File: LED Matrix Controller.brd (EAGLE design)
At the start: 76.2 x 50.8 mm, 5 parts, among them CN1 LED OUT, CN2 5V PWR, U1 328P

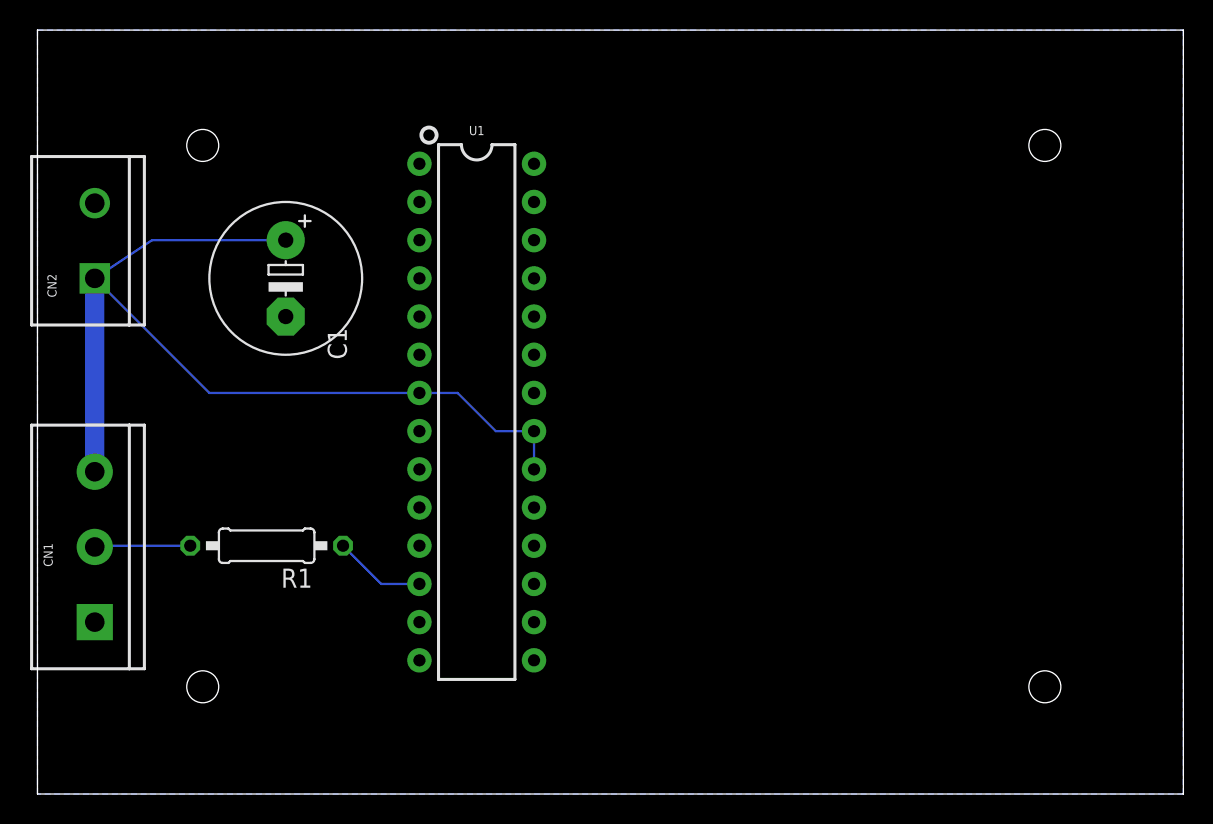
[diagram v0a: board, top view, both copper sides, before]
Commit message: Add ISP and serial debug headers
Somewhat useful for not having to remove the chip to reprogram it.
ISP header needs a wire to connect 5v. I thought that wasn't needed
but once I tested it, apparently it is.
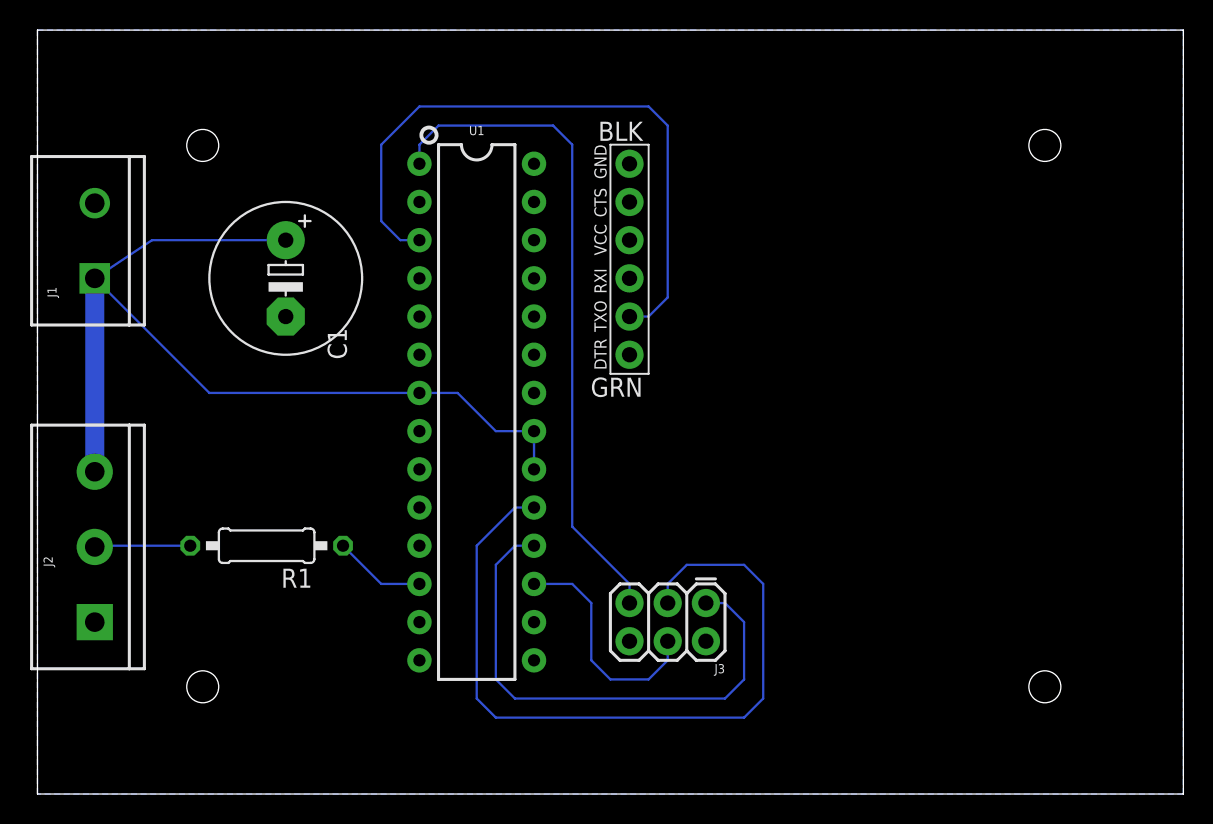
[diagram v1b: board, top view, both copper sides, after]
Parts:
- added J3: AVR ISP, SparkFun-Connectors:2X3
- added J4: SER DBG, SparkFun-Connectors:6_PIN_SERIAL_TARGET_SIDE_W_SILK
- renumbered CN1 to J2, CN2 to J1
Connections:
- new net MISO: J3.1, U1.18
- new net MOSI: J3.4, U1.17
- new net RST: J3.5, U1.1
- new net SCK: J3.3, U1.19
- new net TXD: J4.P$2, U1.3
- net GND: now also J3.6, J4.P$6
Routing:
- net SCK: track 0.00 -> 51.4 mm
- net RST: track 0.00 -> 44.5 mm
- net TXD: track 0.00 -> 43.3 mm
- net MISO: track 0.00 -> 35.1 mm
- net MOSI: track 0.00 -> 15.5 mm
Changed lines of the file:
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@@
 <attribute name="VALUE" x="29.21" y="6.35" size="0.6096" layer="27" font="vector" ratio="20" align="bottom-center"/>
 </element>
-<element name="CN1" library="SparkFun-Connectors" library_urn="urn:adsk.eagle:library:513" package="SCREWTERMINAL-5MM-3" package3d_urn="urn:adsk.eagle:package:38070/1" value="LED OUT" x="3.81" y="11.43" smashed="yes" rot="R90">
+<element name="J2" library="SparkFun-Connectors" library_urn="urn:adsk.eagle:library:513" package="SCREWTERMINAL-5MM-3" package3d_urn="urn:adsk.eagle:package:38070/1" value="LED OUT" x="3.81" y="11.43" smashed="yes" rot="R90">
 <attribute name="NAME" x="1.016" y="15.113" size="0.6096" layer="25" font="vector" ratio="20" rot="R90"/>
 <attribute name="PROD_ID" value="CONN-10134" x="3.81" y="11.43" size="1.778" layer="27" rot="R90" display="off"/>
@@
 <attribute name="VALUE" x="1.905" y="14.859" size="0.6096" layer="27" font="vector" ratio="20" rot="R90"/>
 </element>
-<element name="CN2" library="SparkFun-Connectors" library_urn="urn:adsk.eagle:library:513" package="SCREWTERMINAL-5MM-2" package3d_urn="urn:adsk.eagle:package:38044/1" value="5V PWR" x="3.81" y="34.29" smashed="yes" rot="R90">
+<element name="J1" library="SparkFun-Connectors" library_urn="urn:adsk.eagle:library:513" package="SCREWTERMINAL-5MM-2" package3d_urn="urn:adsk.eagle:package:38044/1" value="5V PWR" x="3.81" y="34.29" smashed="yes" rot="R90">
 <attribute name="NAME" x="1.27" y="33.02" size="0.6096" layer="25" font="vector" ratio="20" rot="R90"/>
 <attribute name="SF_SKU" value="PRT-08432" x="3.81" y="34.29" size="1.778" layer="27" rot="R90" display="off"/>
 <attribute name="VALUE" x="2.54" y="33.02" size="0.6096" layer="27" font="vector" ratio="20" rot="R90"/>
 </element>
+<element name="J3" library="SparkFun-Connectors" library_urn="urn:adsk.eagle:library:513" package="2X3" package3d_urn="urn:adsk.eagle:package:38016/1" value="AVR ISP" x="44.45" y="12.7" smashed="yes" rot="R180">
+<attribute name="NAME" x="45.72" y="8.636" size="0.6096" layer="25" font="vector" ratio="20" rot="R180"/>
+<attribute name="VALUE" x="45.72" y="15.113" size="0.6096" layer="27" font="vector" ratio="20" rot="R180"/>
+</element>
+<element name="J4" library="SparkFun-Connectors" library_urn="urn:adsk.eagle:library:513" package="6_PIN_SERIAL_TARGET_SIDE_W_SILK" package3d_urn="urn:adsk.eagle:package:37995/1" value="SER DBG" x="39.37" y="35.56" smashed="yes" rot="R90"/>
 </elements>
 <signals>
@@
 <wire x1="27.94" y1="26.67" x2="30.48" y2="24.13" width="0.1524" layer="16"/>
 <wire x1="30.48" y1="24.13" x2="33.02" y2="24.13" width="0.1524" layer="16"/>
-<contactref element="CN1" pad="3"/>
-<contactref element="CN2" pad="1"/>
+<contactref element="J2" pad="3"/>
+<contactref element="J1" pad="1"/>
 <contactref element="C1" pad="+"/>
 <wire x1="3.81" y1="34.29" x2="3.81" y2="21.43" width="1.27" layer="16"/>
@@
 <vertex x="0" y="0"/>
 </polygon>
-<contactref element="CN1" pad="1"/>
-<contactref element="CN2" pad="2"/>
+<contactref element="J2" pad="1"/>
+<contactref element="J1" pad="2"/>
 <contactref element="C1" pad="-"/>
+<contactref element="J3" pad="6"/>
+<contactref element="J4" pad="P$6"/>
 </signal>
 <signal name="N$1">
@@
 <signal name="LED_OUT">
 <contactref element="R1" pad="2"/>
-<contactref element="CN1" pad="2"/>
+<contactref element="J2" pad="2"/>
 <wire x1="3.81" y1="16.43" x2="3.89" y2="16.51" width="0.1524" layer="16"/>
 <wire x1="3.89" y1="16.51" x2="10.16" y2="16.51" width="0.1524" layer="16"/>
 </signal>
+<signal name="MOSI">
+<contactref element="U1" pad="17"/>
+<contactref element="J3" pad="4"/>
+<wire x1="33.02" y1="13.97" x2="35.56" y2="13.97" width="0.1524" layer="16"/>
+<wire x1="35.56" y1="13.97" x2="36.83" y2="12.7" width="0.1524" layer="16"/>
+<wire x1="36.83" y1="12.7" x2="36.83" y2="8.89" width="0.1524" layer="16"/>
+<wire x1="36.83" y1="8.89" x2="38.1" y2="7.62" width="0.1524" layer="16"/>
+<wire x1="38.1" y1="7.62" x2="40.64" y2="7.62" width="0.1524" layer="16"/>
+<wire x1="40.64" y1="7.62" x2="41.91" y2="8.89" width="0.1524" layer="16"/>
+<wire x1="41.91" y1="8.89" x2="41.91" y2="10.16" width="0.1524" layer="16"/>
+</signal>
+<signal name="RST">
+<contactref element="U1" pad="1"/>
+<contactref element="J3" pad="5"/>
+<wire x1="25.4" y1="41.91" x2="25.4" y2="43.18" width="0.1524" layer="16"/>
+<wire x1="25.4" y1="43.18" x2="26.67" y2="44.45" width="0.1524" layer="16"/>
+<wire x1="26.67" y1="44.45" x2="34.29" y2="44.45" width="0.1524" layer="16"/>
+<wire x1="34.29" y1="44.45" x2="35.56" y2="43.18" width="0.1524" layer="16"/>
+<wire x1="35.56" y1="43.18" x2="35.56" y2="17.78" width="0.1524" layer="16"/>
+<wire x1="39.37" y1="12.7" x2="39.37" y2="13.97" width="0.1524" layer="16"/>
+<wire x1="39.37" y1="13.97" x2="35.56" y2="17.78" width="0.1524" layer="16"/>
+</signal>
+<signal name="MISO">
+<contactref element="U1" pad="18"/>
+<contactref element="J3" pad="1"/>
+<wire x1="33.02" y1="16.51" x2="31.75" y2="16.51" width="0.1524" layer="16"/>
+<wire x1="31.75" y1="16.51" x2="30.48" y2="15.24" width="0.1524" layer="16"/>
+<wire x1="30.48" y1="15.24" x2="30.48" y2="7.62" width="0.1524" layer="16"/>
+<wire x1="30.48" y1="7.62" x2="31.75" y2="6.35" width="0.1524" layer="16"/>
+<wire x1="31.75" y1="6.35" x2="45.72" y2="6.35" width="0.1524" layer="16"/>
+<wire x1="45.72" y1="6.35" x2="46.99" y2="7.62" width="0.1524" layer="16"/>
+<wire x1="46.99" y1="11.43" x2="45.72" y2="12.7" width="0.1524" layer="16"/>
+<wire x1="45.72" y1="12.7" x2="44.45" y2="12.7" width="0.1524" layer="16"/>
+<wire x1="46.99" y1="7.62" x2="46.99" y2="11.43" width="0.1524" layer="16"/>
+</signal>
+<signal name="SCK">
+<contactref element="U1" pad="19"/>
+<contactref element="J3" pad="3"/>
+<wire x1="33.02" y1="19.05" x2="31.75" y2="19.05" width="0.1524" layer="16"/>
+<wire x1="31.75" y1="19.05" x2="29.21" y2="16.51" width="0.1524" layer="16"/>
+<wire x1="29.21" y1="16.51" x2="29.21" y2="6.35" width="0.1524" layer="16"/>
+<wire x1="29.21" y1="6.35" x2="30.48" y2="5.08" width="0.1524" layer="16"/>
+<wire x1="30.48" y1="5.08" x2="46.99" y2="5.08" width="0.1524" layer="16"/>
+<wire x1="46.99" y1="5.08" x2="48.26" y2="6.35" width="0.1524" layer="16"/>
+<wire x1="48.26" y1="13.97" x2="46.99" y2="15.24" width="0.1524" layer="16"/>
+<wire x1="46.99" y1="15.24" x2="43.18" y2="15.24" width="0.1524" layer="16"/>
+<wire x1="43.18" y1="15.24" x2="41.91" y2="13.97" width="0.1524" layer="16"/>
+<wire x1="41.91" y1="13.97" x2="41.91" y2="12.7" width="0.1524" layer="16"/>
+<wire x1="48.26" y1="6.35" x2="48.26" y2="13.97" width="0.1524" layer="16"/>
+</signal>
+<signal name="TXD">
+<contactref element="U1" pad="3"/>
+<contactref element="J4" pad="P$2"/>
+<wire x1="25.4" y1="36.83" x2="24.13" y2="36.83" width="0.1524" layer="16"/>
+<wire x1="24.13" y1="36.83" x2="22.86" y2="38.1" width="0.1524" layer="16"/>
+<wire x1="22.86" y1="38.1" x2="22.86" y2="43.18" width="0.1524" layer="16"/>
+<wire x1="22.86" y1="43.18" x2="25.4" y2="45.72" width="0.1524" layer="16"/>
+<wire x1="25.4" y1="45.72" x2="40.64" y2="45.72" width="0.1524" layer="16"/>
+<wire x1="40.64" y1="45.72" x2="41.91" y2="44.45" width="0.1524" layer="16"/>
+<wire x1="41.91" y1="44.45" x2="41.91" y2="33.02" width="0.1524" layer="16"/>
+<wire x1="41.91" y1="33.02" x2="40.64" y2="31.75" width="0.1524" layer="16"/>
+<wire x1="40.64" y1="31.75" x2="39.37" y2="31.75" width="0.1524" layer="16"/>
+</signal>
 </signals>

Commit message: Add a reset button
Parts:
- added S1: RESET, SparkFun-Switches:TACTILE_SWITCH_PTH_6.0MM
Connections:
- net GND: now also S1.1
- net RST: now also S1.3
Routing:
- net RST: track 44.5 -> 49.7 mm
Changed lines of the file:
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@@
 </element>
 <element name="J4" library="SparkFun-Connectors" library_urn="urn:adsk.eagle:library:513" package="6_PIN_SERIAL_TARGET_SIDE_W_SILK" package3d_urn="urn:adsk.eagle:package:37995/1" value="SER DBG" x="39.37" y="35.56" smashed="yes" rot="R90"/>
+<element name="S1" library="SparkFun-Switches" library_urn="urn:adsk.eagle:library:535" package="TACTILE_SWITCH_PTH_6.0MM" package3d_urn="urn:adsk.eagle:package:40163/1" value="RESET" x="41.91" y="21.59" smashed="yes">
+<attribute name="NAME" x="41.91" y="24.892" size="0.6096" layer="25" font="vector" ratio="20" align="bottom-center"/>
+<attribute name="PROD_ID" value=" SWCH-08441" x="41.91" y="21.59" size="1.778" layer="27" display="off"/>
+<attribute name="SF_SKU" value="COM-00097" x="41.91" y="21.59" size="1.778" layer="27" display="off"/>
+<attribute name="VALUE" x="41.91" y="18.415" size="0.6096" layer="27" font="vector" ratio="20" align="top-center"/>
+</element>
 </elements>
 <signals>
@@
 <contactref element="J3" pad="6"/>
 <contactref element="J4" pad="P$6"/>
+<contactref element="S1" pad="1"/>
 </signal>
 <signal name="N$1">
@@
 <wire x1="34.29" y1="44.45" x2="35.56" y2="43.18" width="0.1524" layer="16"/>
 <wire x1="35.56" y1="43.18" x2="35.56" y2="17.78" width="0.1524" layer="16"/>
-<wire x1="39.37" y1="12.7" x2="39.37" y2="13.97" width="0.1524" layer="16"/>
-<wire x1="39.37" y1="13.97" x2="35.56" y2="17.78" width="0.1524" layer="16"/>
+<contactref element="S1" pad="3"/>
+<wire x1="38.6588" y1="19.3294" x2="39.37" y2="18.6182" width="0.1524" layer="16"/>
+<wire x1="39.37" y1="18.6182" x2="39.37" y2="15.24" width="0.1524" layer="16"/>
+<wire x1="35.56" y1="17.78" x2="38.1" y2="15.24" width="0.1524" layer="16"/>
+<wire x1="38.1" y1="15.24" x2="39.37" y2="15.24" width="0.1524" layer="16"/>
+<wire x1="39.37" y1="12.7" x2="39.37" y2="15.24" width="0.1524" layer="16"/>
 </signal>
 <signal name="MISO">

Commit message: Replace ATmega328P with ESP32 dev board
Quick and dirty routing to stick a DOIT ESP32 dev module on the
board. No attention given to RF keepout.
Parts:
- removed J3: AVR ISP, SparkFun-Connectors:2X3
- removed U1: 328P, SparkFun-IC-Microcontroller:DIP28
- added U$1: ESP32_DEVKIT, DOIT_ESP32_DEVKIT:ESP32_DEVKIT
- moved S1 29.6 mm to (16.5, 36.8), turned to 180 degrees
- moved J4 21.7 mm to (61.0, 38.1)
- moved C1 10.2 mm to (16.5, 24.1)
- moved R1 3.81 mm to (15.2, 12.7)
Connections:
- removed net MISO: J3.1, U1.18
- removed net MOSI: J3.4, U1.17
- removed net SCK: J3.3, U1.19
- net +5V: now also U$1.VIN; no longer U1.20, U1.21, U1.7
- net GND: now also U$1.GND@1, U$1.GND@2; no longer J3.6, U1.22, U1.8
- net N$1: now also U$1.D27; no longer U1.12
- net RST: now also U$1.EN; no longer J3.5, U1.1
- net TXD: now also U$1.TX0; no longer U1.3
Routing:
- net SCK: track 51.4 -> 0.00 mm
- net RST: track 49.7 -> 9.13 mm
- net MISO: track 35.1 -> 0.00 mm
- net TXD: track 43.3 -> 11.0 mm
- net MOSI: track 15.5 -> 0.00 mm
- net +5V: track 62.3 -> 69.5 mm
- net N$1: track 6.13 -> 12.3 mm
- net LED_OUT: track 6.38 -> 7.90 mm

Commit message: Add a 74HCT245 as a level shifter
The ESP32 uses 3.3v logic, and even though it "worked" on my test
board, it's possible that I was just lucky. The Internet wants me to
use this chip, even though I'm wasting 7 buffers for a single I/O.

I'd like to build up one of these, but I will probably change it later
for something smaller.
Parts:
- added IC1: 74HCT245N, 74xx-eu:DIL20
- moved J4 15.3 mm to (71.1, 26.7)
- moved U$1 11.4 mm to (52.1, 26.7)
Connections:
- new net N$2: IC1.2, R1.1
- net +5V: now also IC1.20
- net GND: now also IC1.1, IC1.10, IC1.11, IC1.12, IC1.13, IC1.14, IC1.15, IC1.16, IC1.17, IC1.19
- net N$1: now also IC1.18; no longer R1.1
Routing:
- net +5V: track 69.5 -> 107.2 mm
- net N$2: track 0.00 -> 24.0 mm
- net RST: track 9.13 -> 20.6 mm
- net TXD: track 11.0 -> 22.0 mm
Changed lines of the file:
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@@
 <param name="TopRouterVariant" value="1"/>
 <param name="tpViaShape" value="round"/>
-<param name="PrefDir.1" value="a"/>
+<param name="PrefDir.1" value="0"/>
 <param name="PrefDir.2" value="0"/>
 <param name="PrefDir.3" value="0"/>
@@
 <attribute name="VALUE" x="2.54" y="33.02" size="0.6096" layer="27" font="vector" ratio="20" rot="R90"/>
 </element>
-<element name="J4" library="SparkFun-Connectors" library_urn="urn:adsk.eagle:library:513" package="6_PIN_SERIAL_TARGET_SIDE_W_SILK" package3d_urn="urn:adsk.eagle:package:37995/1" value="SER DBG" x="60.96" y="38.1" smashed="yes" rot="R90"/>
+<element name="J4" library="SparkFun-Connectors" library_urn="urn:adsk.eagle:library:513" package="6_PIN_SERIAL_TARGET_SIDE_W_SILK" package3d_urn="urn:adsk.eagle:package:37995/1" value="SER DBG" x="71.12" y="26.67" smashed="yes" rot="R90"/>
 <element name="S1" library="SparkFun-Switches" library_urn="urn:adsk.eagle:library:535" package="TACTILE_SWITCH_PTH_6.0MM" package3d_urn="urn:adsk.eagle:package:40163/1" value="RESET" x="16.51" y="36.83" smashed="yes" rot="R180">
 <attribute name="NAME" x="16.51" y="33.528" size="0.6096" layer="25" font="vector" ratio="20" rot="R180" align="bottom-center"/>
@@
 <attribute name="VALUE" x="16.51" y="40.005" size="0.6096" layer="27" font="vector" ratio="20" rot="R180" align="top-center"/>
 </element>
-<element name="U$1" library="DOIT_ESP32_DEVKIT" package="ESP32_DEVKIT" value="ESP32_DEVKIT" x="40.64" y="26.67" smashed="yes">
-<attribute name="NAME" x="35.56" y="5.08" size="1.778" layer="25" rot="R90"/>
-<attribute name="VALUE" x="44.45" y="5.08" size="1.778" layer="27" rot="R90"/>
+<element name="U$1" library="DOIT_ESP32_DEVKIT" package="ESP32_DEVKIT" value="ESP32_DEVKIT" x="52.07" y="26.67" smashed="yes">
+<attribute name="NAME" x="46.99" y="5.08" size="1.778" layer="25" rot="R90"/>
+<attribute name="VALUE" x="55.88" y="5.08" size="1.778" layer="27" rot="R90"/>
+</element>
+<element name="IC1" library="74xx-eu" library_urn="urn:adsk.eagle:library:85" package="DIL20" package3d_urn="urn:adsk.eagle:package:16429/2" value="74HCT245N" x="29.21" y="25.4" smashed="yes" rot="R270">
+<attribute name="NAME" x="26.162" y="38.481" size="1.27" layer="25"/>
+<attribute name="POPULARITY" value="1" x="29.21" y="25.4" size="1.778" layer="27" rot="R270" display="off"/>
+<attribute name="VALUE" x="28.829" y="35.179" size="1.27" layer="27" rot="R270"/>
 </element>
 </elements>
@@
 <wire x1="15.24" y1="15.24" x2="15.24" y2="10.16" width="0.1524" layer="16"/>
 <wire x1="15.24" y1="10.16" x2="16.51" y2="8.89" width="0.1524" layer="16"/>
-<wire x1="16.51" y1="8.89" x2="26.67" y2="8.89" width="0.1524" layer="16"/>
+<wire x1="16.51" y1="8.89" x2="38.1" y2="8.89" width="0.1524" layer="16"/>
+<contactref element="IC1" pad="20"/>
+<wire x1="31.3182" y1="36.8046" x2="32.9184" y2="36.8046" width="0.1524" layer="16"/>
+<wire x1="28.448" y1="39.6748" x2="31.3182" y2="36.8046" width="0.1524" layer="16"/>
+<wire x1="24.2316" y1="39.6748" x2="28.448" y2="39.6748" width="0.1524" layer="16"/>
+<wire x1="22.098" y1="37.5412" x2="24.2316" y2="39.6748" width="0.1524" layer="16"/>
+<wire x1="22.098" y1="32.6136" x2="22.098" y2="37.5412" width="0.1524" layer="16"/>
+<wire x1="16.6878" y1="27.2034" x2="22.098" y2="32.6136" width="0.1524" layer="16"/>
+<wire x1="16.6878" y1="26.7462" x2="16.6878" y2="27.2034" width="0.1524" layer="16"/>
+<wire x1="32.9184" y1="36.8046" x2="33.02" y2="36.83" width="0.1524" layer="16"/>
+<wire x1="16.6878" y1="26.7462" x2="16.51" y2="26.67" width="0.1524" layer="16"/>
 </signal>
 <signal name="GND">
@@
 <contactref element="U$1" pad="GND@2"/>
 <contactref element="U$1" pad="GND@1"/>
-</signal>
-<signal name="N$1">
-<contactref element="R1" pad="1"/>
-<contactref element="U$1" pad="D27"/>
-<wire x1="20.32" y1="12.7" x2="20.32" y2="16.51" width="0.1524" layer="16"/>
-<wire x1="20.32" y1="16.51" x2="25.4" y2="21.59" width="0.1524" layer="16"/>
-<wire x1="25.4" y1="21.59" x2="26.67" y2="21.59" width="0.1524" layer="16"/>
+<contactref element="IC1" pad="10"/>
+<contactref element="IC1" pad="1"/>
+<contactref element="IC1" pad="19"/>
+<contactref element="IC1" pad="17"/>
+<contactref element="IC1" pad="16"/>
+<contactref element="IC1" pad="15"/>
+<contactref element="IC1" pad="14"/>
+<contactref element="IC1" pad="13"/>
+<contactref element="IC1" pad="12"/>
+<contactref element="IC1" pad="11"/>
 </signal>
 <signal name="LED_OUT">
@@
 <contactref element="U$1" pad="EN"/>
 <wire x1="19.7612" y1="39.0906" x2="25.1206" y2="44.45" width="0.1524" layer="16"/>
-<wire x1="25.1206" y1="44.45" x2="26.67" y2="44.45" width="0.1524" layer="16"/>
+<wire x1="25.1206" y1="44.45" x2="38.1" y2="44.45" width="0.1524" layer="16"/>
 </signal>
 <signal name="TXD">
 <contactref element="J4" pad="P$2"/>
 <contactref element="U$1" pad="TX0"/>
-<wire x1="52.07" y1="39.37" x2="53.34" y2="39.37" width="0.1524" layer="16"/>
-<wire x1="58.42" y1="34.29" x2="60.96" y2="34.29" width="0.1524" layer="16"/>
-<wire x1="53.34" y1="39.37" x2="58.42" y2="34.29" width="0.1524" layer="16"/>
+<wire x1="66.7258" y1="37.4142" x2="64.77" y2="39.37" width="0.1524" layer="16"/>
+<wire x1="64.77" y1="39.37" x2="63.5" y2="39.37" width="0.1524" layer="16"/>
+<wire x1="66.7258" y1="24.4602" x2="66.7258" y2="37.4142" width="0.1524" layer="16"/>
+<wire x1="68.326" y1="22.86" x2="66.7258" y2="24.4602" width="0.1524" layer="16"/>
+<wire x1="71.12" y1="22.86" x2="68.326" y2="22.86" width="0.1524" layer="16"/>
+</signal>
+<signal name="N$1">
+<contactref element="IC1" pad="18"/>
+<contactref element="U$1" pad="D27"/>
+<wire x1="33.8328" y1="31.5468" x2="33.147" y2="31.5468" width="0.1524" layer="16"/>
+<wire x1="35.5854" y1="29.7942" x2="33.8328" y2="31.5468" width="0.1524" layer="16"/>
+<wire x1="35.5854" y1="24.3078" x2="35.5854" y2="29.7942" width="0.1524" layer="16"/>
+<wire x1="38.1762" y1="21.717" x2="35.5854" y2="24.3078" width="0.1524" layer="16"/>
+<wire x1="33.147" y1="31.5468" x2="33.02" y2="31.75" width="0.1524" layer="16"/>
+<wire x1="38.1762" y1="21.717" x2="38.1" y2="21.59" width="0.1524" layer="16"/>
+</signal>
+<signal name="N$2">
+<contactref element="R1" pad="1"/>
+<contactref element="IC1" pad="2"/>
+<wire x1="23.0886" y1="15.5448" x2="20.3454" y2="12.8016" width="0.1524" layer="16"/>
+<wire x1="23.0886" y1="32.4612" x2="23.0886" y2="15.5448" width="0.1524" layer="16"/>
+<wire x1="24.9174" y1="34.29" x2="23.0886" y2="32.4612" width="0.1524" layer="16"/>
+<wire x1="25.4" y1="34.29" x2="24.9174" y2="34.29" width="0.1524" layer="16"/>
+<wire x1="20.3454" y1="12.8016" x2="20.32" y2="12.7" width="0.1524" layer="16"/>
 </signal>
 </signals>
